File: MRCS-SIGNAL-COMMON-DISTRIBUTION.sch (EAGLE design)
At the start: 10 parts, among them CON1 DC PWR, CON2 DC PWR

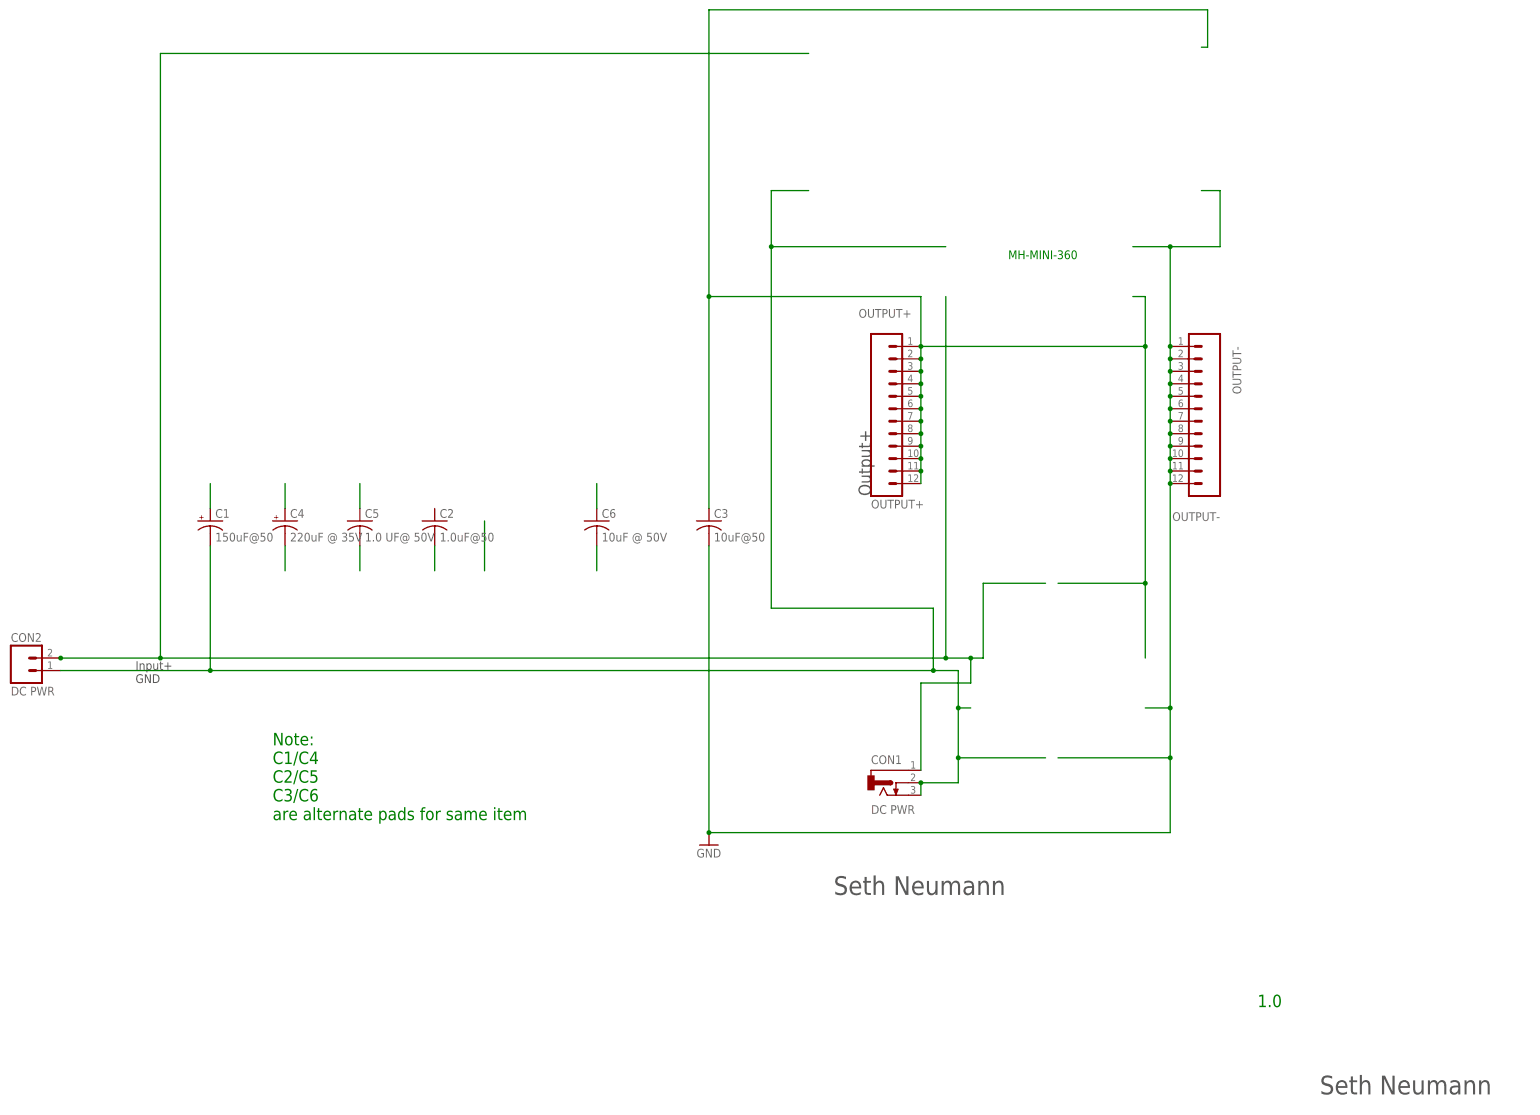
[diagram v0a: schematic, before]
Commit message: initial board for testing
first pass, this is based on the Buckeroo footprint
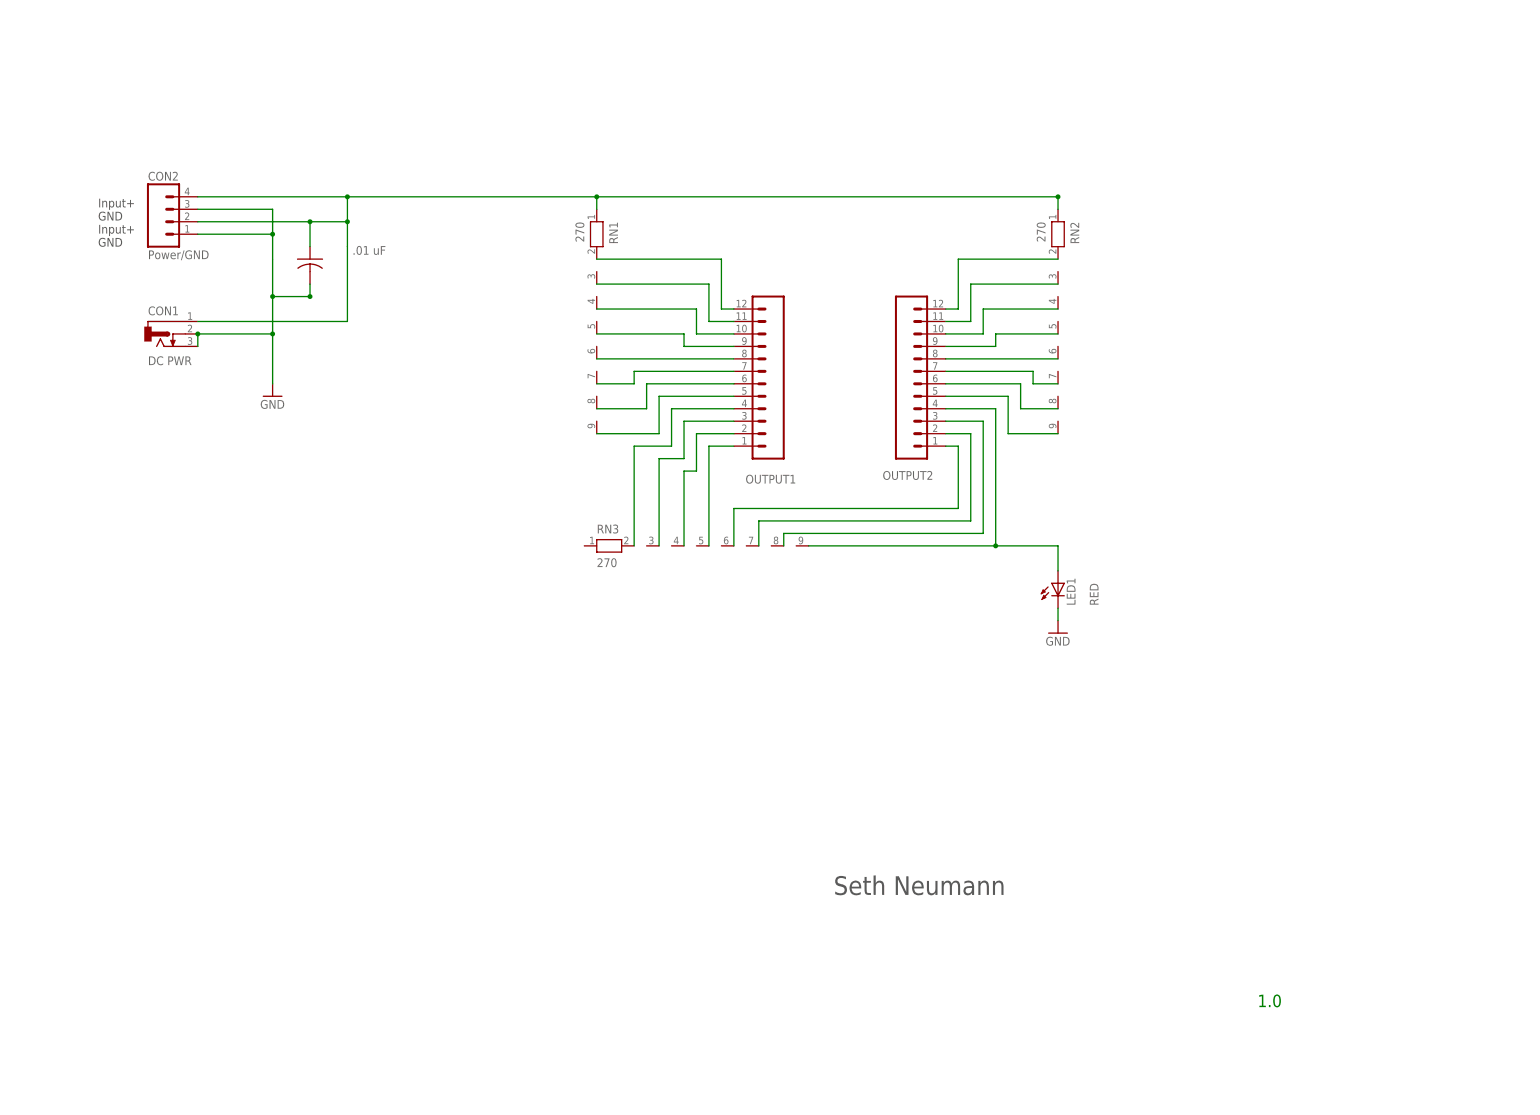
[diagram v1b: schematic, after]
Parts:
- removed C2: 1.0uF@50, SPCoast:CAPPTH2
- removed C3: 10uF@50, SPCoast:CAPPTH2
- removed C4: 220uF @ 35V, SPCoast:CAP-POLPTH-2.5MM
- removed C5: 1.0 UF@ 50V, SPCoast:CAPPTH1
- removed C6: 10uF @ 50V, SPCoast:CAPPTH1
- removed OUTPUT+: OUTPUT+, SPCoast:CONNECTOR-M12LOCK
- removed OUTPUT-: OUTPUT-, SPCoast:CONNECTOR-M12LOCK
- added CON3: OUTPUT1, SPCoast:CONNECTOR-M12LOCK
- added CON4: OUTPUT2, SPCoast:CONNECTOR-M12LOCK
- added LED1: RED, SPCoast:LEDLED3MM
- added RN1, RN2, RN3: 270, resistor-net:RN08
- C1: value 150uF@50 -> .01 uF; device SPCoast:CAP-POLPTH-5MM -> SPCoast:CAPPTH1
- CON2: value DC PWR -> Power/GND; device SPCoast:CONNECTOR-M023.5MM-LOCK -> SPCoast:CONNECTOR-M04SCREW_LOCK
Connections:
- removed net OUTPUT+: C3.1, OUTPUT+.1, OUTPUT+.10, OUTPUT+.11, OUTPUT+.12, OUTPUT+.2, OUTPUT+.3, OUTPUT+.4, OUTPUT+.5, OUTPUT+.6, OUTPUT+.7, OUTPUT+.8, OUTPUT+.9
- new net N$10: CON4.11, RN2.3
- new net N$11: CON4.10, RN2.4
- new net N$12: CON4.9, RN2.5
- new net N$13: CON4.8, RN2.6
- new net N$14: CON4.7, RN2.7
- new net N$15: CON4.6, RN2.8
- new net N$16: CON4.5, RN2.9
- new net N$17: CON3.4, RN3.2
- new net N$18: CON3.3, RN3.3
- new net N$19: CON3.2, RN3.4
- new net N$20: CON3.1, RN3.5
- new net N$21: CON4.1, RN3.6
- new net N$22: CON4.4, LED1.A, RN3.9
- new net N$23: CON4.3, RN3.8
- new net N$24: CON4.2, RN3.7
- new net N$7: CON3.6, RN1.8
- net GND: now also C1.2, CON2.1, CON2.3, LED1.C; no longer C1.-, C3.2, CON2.A, OUTPUT-.1, OUTPUT-.10, OUTPUT-.11, OUTPUT-.12, OUTPUT-.2, OUTPUT-.3, OUTPUT-.4, OUTPUT-.5, OUTPUT-.6, OUTPUT-.7, OUTPUT-.8, OUTPUT-.9
- net INPUT+: now also C1.1, CON2.2, CON2.4, RN1.1, RN2.1; no longer CON2.B
- net N$1: now also CON3.12, RN1.2; no longer C5.1
- net N$2: now also CON3.11, RN1.3; no longer C4.+
- net N$3: now also CON3.10, RN1.4; no longer C1.+
- net N$4: now also CON3.9, RN1.5; no longer C2.2
- net N$5: now also CON3.8, RN1.6; no longer C4.-
- net N$6: now also CON3.7, RN1.7; no longer C5.2
- net N$8: now also CON3.5, RN1.9; no longer C6.2
- net N$9: now also CON4.12, RN2.2; no longer C6.1
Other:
- note added: "Input+ GND Input+ GND"
- note removed: "Input+ GND"
- note removed: "MH-MINI-360"
- note removed: "Note: C1/C4 C2/C5 C3/C6 are alternate pads for same item"
- note removed: "Output+"
- moved on the sheet: CON1
